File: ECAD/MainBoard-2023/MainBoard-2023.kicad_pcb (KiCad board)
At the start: 2 copper layers, 60 x 150 mm, 84 parts, among them J1 XT60, J10 Conn_01x14, J11 Conn_01x03, J12 Conn_01x04, J13 Conn_01x03, J14 Conn_01x03, J15 Conn_01x03, J16 XT30, J17 XT30, J2 Conn_01x04, J20 BAU, J21 BAU, J22 Conn_01x04, J23 Conn_01x02, J24 Conn_01x07, J26 BAU, J27 BAU, J28 Conn_01x02, J29 Conn_01x02, J3 ConStep1, J30 Conn_01x03, J32 Conn_01x02, J37 Conn_01x02, J38 Conn_01x02, J39 Conn_01x02, J4 Conn_01x02, J40 Conn_01x02, J5 ConStep1, J6 ConStep1, J7 XT30, J8 Conn_01x02, J9 XT60, K1 CB1-P-24V, U1 Teensy3.5_All_Pins, U2 R-78B3.3-2.0, U4 R-78B5.0-2.0

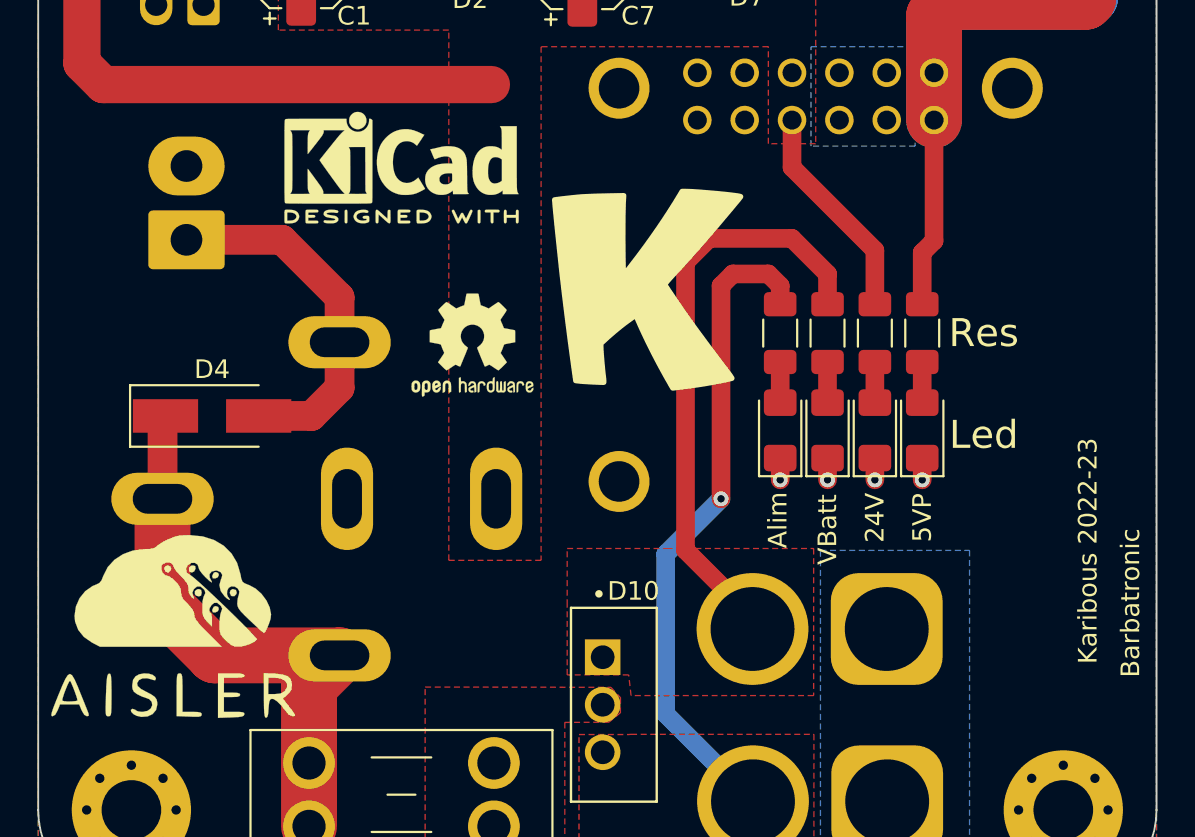
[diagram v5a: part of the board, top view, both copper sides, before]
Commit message: add silkscreen elements
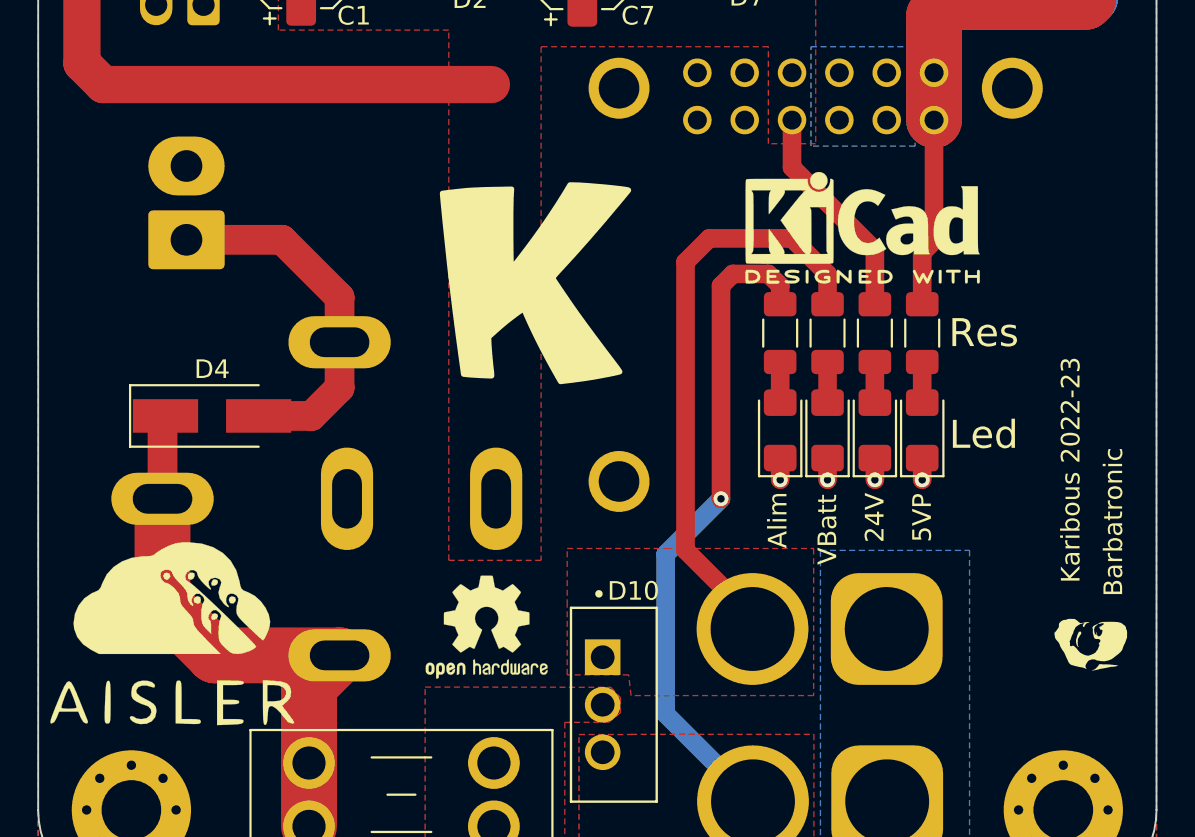
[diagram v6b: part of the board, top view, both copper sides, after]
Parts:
- added G***: LOGO, LOGO, B.Cu at (119.9, 46.4)
- added G***: LOGO, LOGO, F.Cu at (147.5, 162.2)
- added G***: LOGO, LOGO, B.Cu at (112.1, 30.3)
- added G***: LOGO, LOGO, B.Cu at (140.3, 34.3)
- added G***: LOGO, LOGO, B.Cu at (108.4, 47.5)
- moved REF** 24.9 mm to (135.2, 139.8)
- moved REF** 15.2 mm to (115.1, 161.2)
- moved G*** 0.39 mm to (98.4, 161.7)
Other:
- board text added: "Connecteur Actionneurs"
- board text added: "D+"
- board text added: "D-"
- board text added: "I2C"
- board text added: "Lidar"
- board text added: "NeoPixel"
- board text added: "SCL"
- board text added: "SDA"
- board text added: "Sig"
- board text added: "USB"
- board text added: "Xbee"
